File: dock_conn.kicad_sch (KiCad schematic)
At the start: 2 parts, among them J10 Conn_02x35_Odd_Even

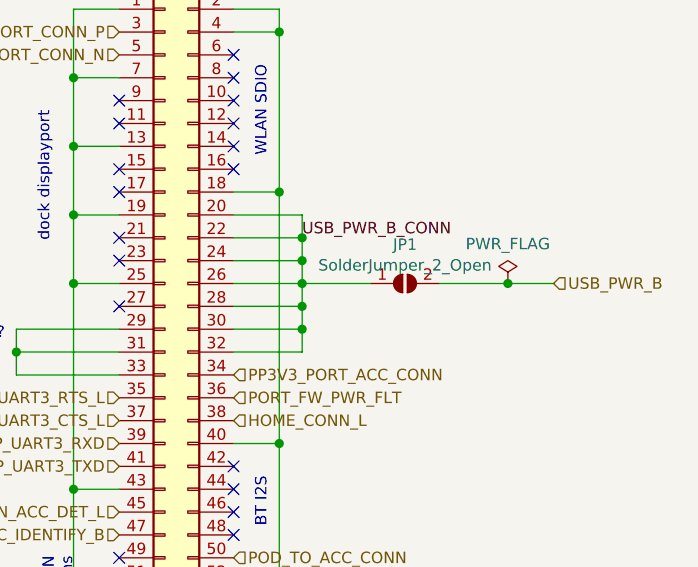
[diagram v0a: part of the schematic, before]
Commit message: Update to Kicad 6.0.0
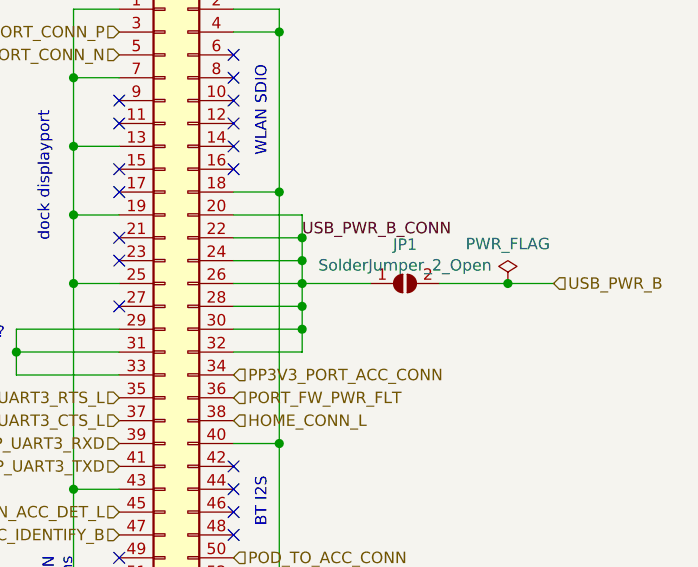
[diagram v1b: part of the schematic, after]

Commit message: Lots more work on the cm3 version of this board.
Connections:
- net DP_TX_1N: now reaches J10.11 (Pin_11)
- net DP_TX_0N: now reaches J10.15 (Pin_15)
- net DP_TX_0P: now reaches J10.17 (Pin_17)
- net DP_AUX_P: now reaches J10.21 (Pin_21)
- net DP_AUX_N: now reaches J10.23 (Pin_23)
- net DP_TX_1P: now reaches J10.9 (Pin_9)
- no-connect marks 24 -> 18
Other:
- note added: "yep, DP_TX_0N/P are supposed to have the reverse polarity from the other two pairs"
- note removed: "dock displayport"
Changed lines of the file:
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@@
   (junction (at 149.86 133.35) (diameter 1.016) (color 0 0 0 0)
   )
-  (no_connect (at 132.08 57.15))
-  (no_connect (at 132.08 59.69))
-  (no_connect (at 132.08 64.77))
-  (no_connect (at 132.08 67.31))
-  (no_connect (at 132.08 72.39))
-  (no_connect (at 132.08 74.93))
   (no_connect (at 132.08 107.95))
   (no_connect (at 132.08 110.49))
@@
     (effects (font (size 1.27 1.27)) (justify right bottom))
   )
-  (text "dock displayport" (at 124.46 58.42 270)
-    (effects (font (size 1.27 1.27)) (justify right bottom))
-  )
   (text "I guess WL means wireless link?" (at 119.38 83.82 180)
+    (effects (font (size 1.27 1.27)) (justify right bottom))
+  )
+  (text "yep, DP_TX_0N/P are supposed\nto have the reverse polarity\nfrom the other two pairs"
+    (at 120.65 68.58 0)
     (effects (font (size 1.27 1.27)) (justify right bottom))
   )
@@
     (effects (font (size 1.27 1.27)) (justify right))
   )
+  (hierarchical_label "DP_TX_1N" (shape input) (at 132.08 59.69 180)
+    (effects (font (size 1.27 1.27)) (justify right))
+  )
   (hierarchical_label "POD_TO_ACC_CONN" (shape input) (at 144.78 107.95 0)
     (effects (font (size 1.27 1.27)) (justify left))
@@
     (effects (font (size 1.27 1.27)) (justify left))
   )
+  (hierarchical_label "DP_AUX_N" (shape input) (at 132.08 74.93 180)
+    (effects (font (size 1.27 1.27)) (justify right))
+  )
   (hierarchical_label "PP3V3_PORT_ACC_CONN" (shape input) (at 144.78 87.63 0)
     (effects (font (size 1.27 1.27)) (justify left))
@@
     (effects (font (size 1.27 1.27)) (justify right))
   )
+  (hierarchical_label "DP_TX_1P" (shape input) (at 132.08 57.15 180)
+    (effects (font (size 1.27 1.27)) (justify right))
+  )
   (hierarchical_label "PP1V8_X17" (shape input) (at 132.08 120.65 180)
     (effects (font (size 1.27 1.27)) (justify right))
@@
     (effects (font (size 1.27 1.27)) (justify right))
   )
+  (hierarchical_label "DP_TX_0P" (shape input) (at 132.08 67.31 180)
+    (effects (font (size 1.27 1.27)) (justify right))
+  )
+  (hierarchical_label "DP_AUX_P" (shape input) (at 132.08 72.39 180)
+    (effects (font (size 1.27 1.27)) (justify right))
+  )
   (hierarchical_label "GND_AUDIO_DOCKB" (shape input) (at 118.11 123.19 180)
     (effects (font (size 1.27 1.27)) (justify right))
@@
     (effects (font (size 1.27 1.27)) (justify right))
   )
+  (hierarchical_label "DP_TX_0N" (shape input) (at 132.08 64.77 180)
+    (effects (font (size 1.27 1.27)) (justify right))
+  )
